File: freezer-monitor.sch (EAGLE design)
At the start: 7 parts, among them J1 1X2-3.5MM

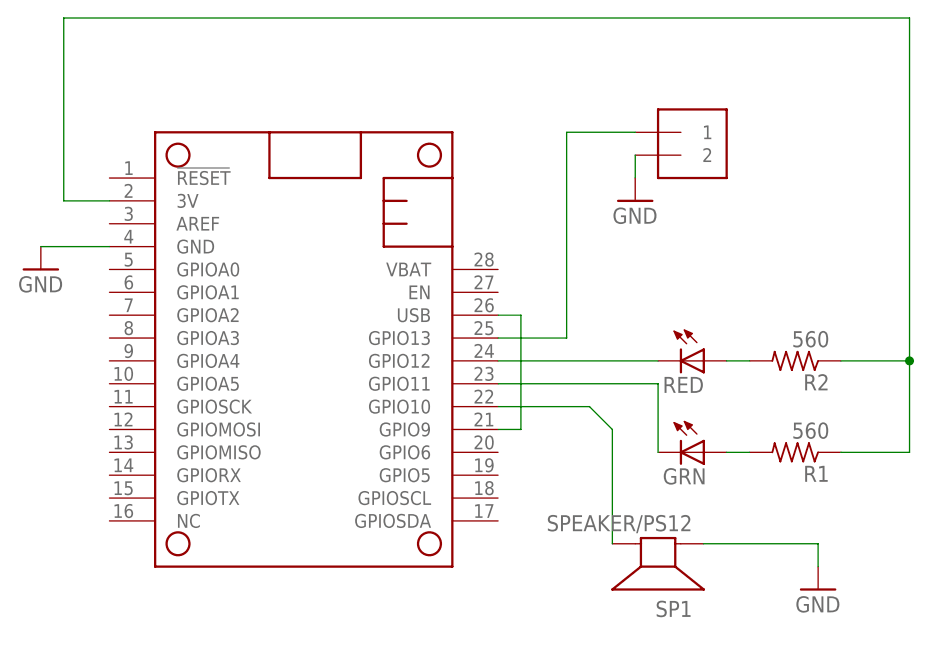
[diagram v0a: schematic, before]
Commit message: Revert "Add line from USB to logic in"
This reverts commit aa022d101621f46ab4c7c753449e8c0f6e997a72.
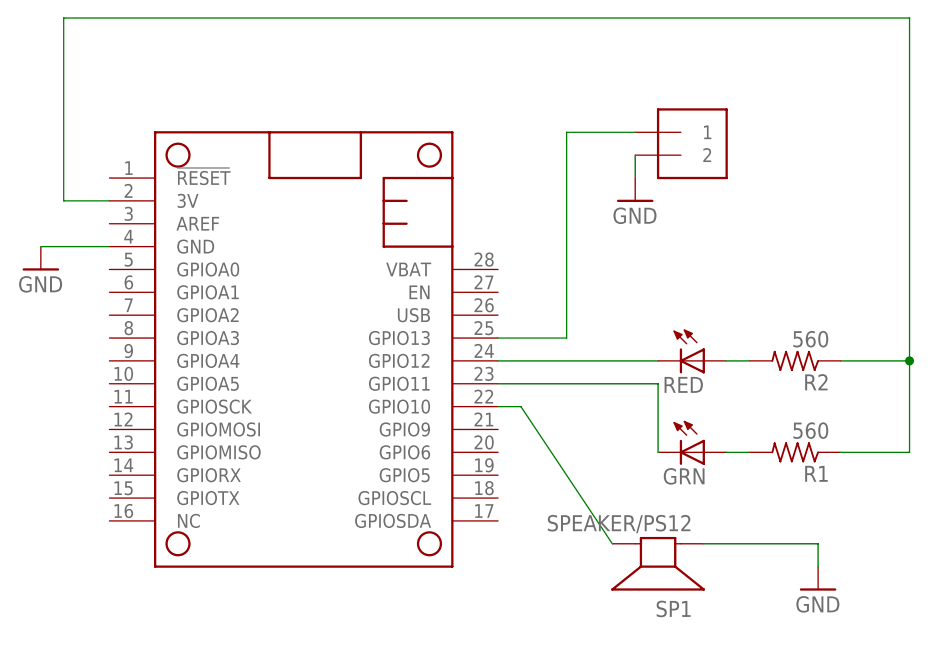
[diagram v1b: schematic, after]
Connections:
- removed net USB: MS1.GPIO9, MS1.USB
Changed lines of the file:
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@@
 <?xml version="1.0" encoding="utf-8"?>
 <!DOCTYPE eagle SYSTEM "eagle.dtd">
-<eagle version="9.1.3">
+<eagle version="8.2.2">
 <drawing>
 <settings>
-<setting alwaysvectorfont="yes"/>
-<setting keepoldvectorfont="yes"/>
+<setting alwaysvectorfont="no"/>
 <setting verticaltext="up"/>
 </settings>
@@
 <segment>
 <pinref part="MS1" gate="G$1" pin="GPIO10"/>
+<pinref part="SP1" gate="S1" pin="-"/>
 <wire x1="60.96" y1="38.1" x2="63.5" y2="38.1" width="0.1524" layer="91"/>
-<wire x1="63.5" y1="38.1" x2="71.12" y2="38.1" width="0.1524" layer="91"/>
-<pinref part="SP1" gate="S1" pin="-"/>
-<wire x1="71.12" y1="38.1" x2="73.66" y2="35.56" width="0.1524" layer="91"/>
-<wire x1="73.66" y1="35.56" x2="73.66" y2="22.86" width="0.1524" layer="91"/>
+<wire x1="63.5" y1="38.1" x2="73.66" y2="22.86" width="0.1524" layer="91"/>
 </segment>
 </net>
@@
 </segment>
 </net>
-<net name="USB" class="0">
-<segment>
-<pinref part="MS1" gate="G$1" pin="USB"/>
-<wire x1="60.96" y1="48.26" x2="63.5" y2="48.26" width="0.1524" layer="91"/>
-<wire x1="63.5" y1="48.26" x2="63.5" y2="35.56" width="0.1524" layer="91"/>
-<pinref part="MS1" gate="G$1" pin="GPIO9"/>
-<wire x1="63.5" y1="35.56" x2="60.96" y2="35.56" width="0.1524" layer="91"/>
-</segment>
-</net>
 </nets>
 </sheet>
@@
 <compatibility>
 <note version="8.2" severity="warning">
-Since Version 8.2, EAGLE supports online libraries. The ids
+Since Version 8.2, Eagle supports online libraries. The ids
 of those online libraries will not be understood (or retained)
 with this version.

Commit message: Add line from USB to logic in
Update to bring power from USB port to logic in.  This so we can add the ability to text when the power is out.
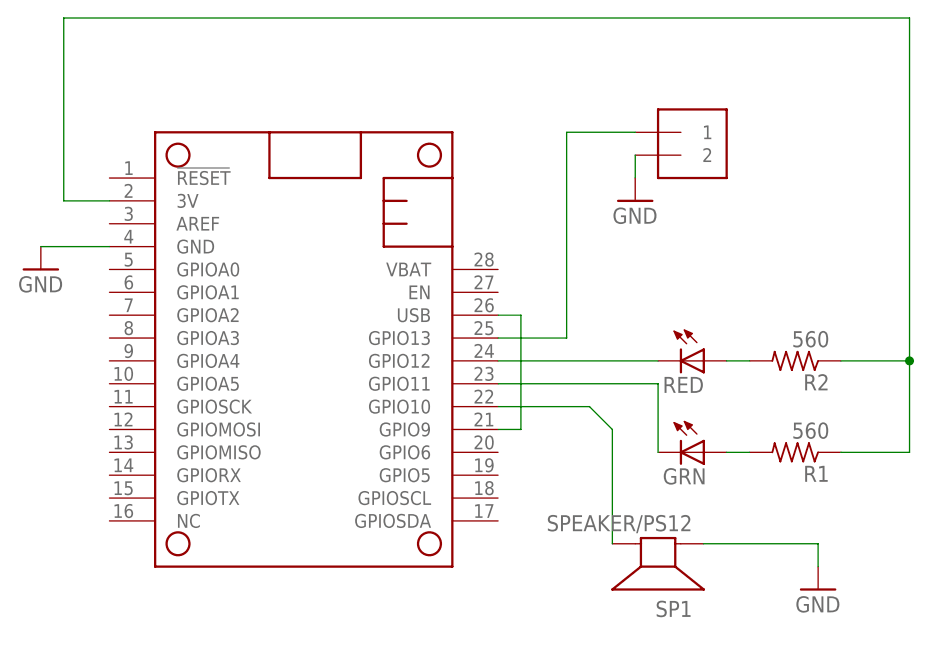
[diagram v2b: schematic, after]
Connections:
- new net USB: MS1.GPIO9, MS1.USB
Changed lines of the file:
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@@
 <?xml version="1.0" encoding="utf-8"?>
 <!DOCTYPE eagle SYSTEM "eagle.dtd">
-<eagle version="8.2.2">
+<eagle version="9.1.3">
 <drawing>
 <settings>
-<setting alwaysvectorfont="no"/>
+<setting alwaysvectorfont="yes"/>
+<setting keepoldvectorfont="yes"/>
 <setting verticaltext="up"/>
 </settings>
@@
 <segment>
 <pinref part="MS1" gate="G$1" pin="GPIO10"/>
+<wire x1="60.96" y1="38.1" x2="63.5" y2="38.1" width="0.1524" layer="91"/>
+<wire x1="63.5" y1="38.1" x2="71.12" y2="38.1" width="0.1524" layer="91"/>
 <pinref part="SP1" gate="S1" pin="-"/>
-<wire x1="60.96" y1="38.1" x2="63.5" y2="38.1" width="0.1524" layer="91"/>
-<wire x1="63.5" y1="38.1" x2="73.66" y2="22.86" width="0.1524" layer="91"/>
+<wire x1="71.12" y1="38.1" x2="73.66" y2="35.56" width="0.1524" layer="91"/>
+<wire x1="73.66" y1="35.56" x2="73.66" y2="22.86" width="0.1524" layer="91"/>
 </segment>
 </net>
@@
 </segment>
 </net>
+<net name="USB" class="0">
+<segment>
+<pinref part="MS1" gate="G$1" pin="USB"/>
+<wire x1="60.96" y1="48.26" x2="63.5" y2="48.26" width="0.1524" layer="91"/>
+<wire x1="63.5" y1="48.26" x2="63.5" y2="35.56" width="0.1524" layer="91"/>
+<pinref part="MS1" gate="G$1" pin="GPIO9"/>
+<wire x1="63.5" y1="35.56" x2="60.96" y2="35.56" width="0.1524" layer="91"/>
+</segment>
+</net>
 </nets>
 </sheet>
@@
 <compatibility>
 <note version="8.2" severity="warning">
-Since Version 8.2, Eagle supports online libraries. The ids
+Since Version 8.2, EAGLE supports online libraries. The ids
 of those online libraries will not be understood (or retained)
 with this version.
